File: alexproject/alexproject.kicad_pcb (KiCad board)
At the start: 2 copper layers, 22.4 x 27.9 mm, 20 parts, among them J1 Conn_01x03_Pin, Q1 NMOS, Q2 NMOS

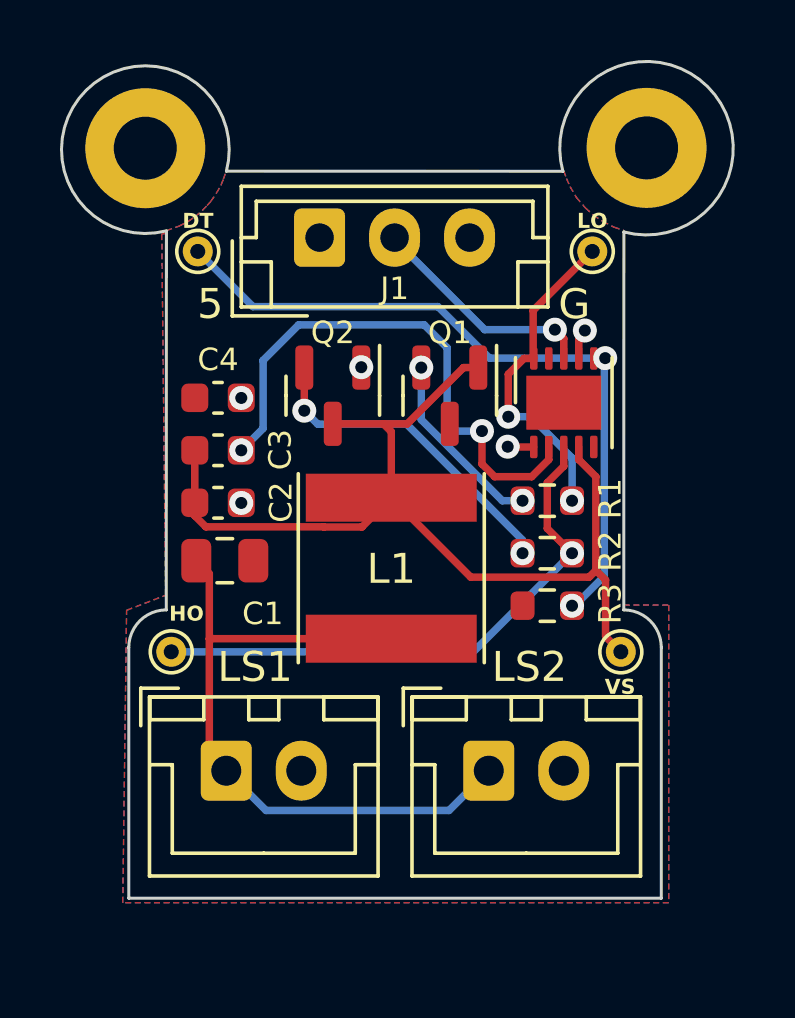
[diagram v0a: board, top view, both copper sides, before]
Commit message: testing spice sim & updated PCB
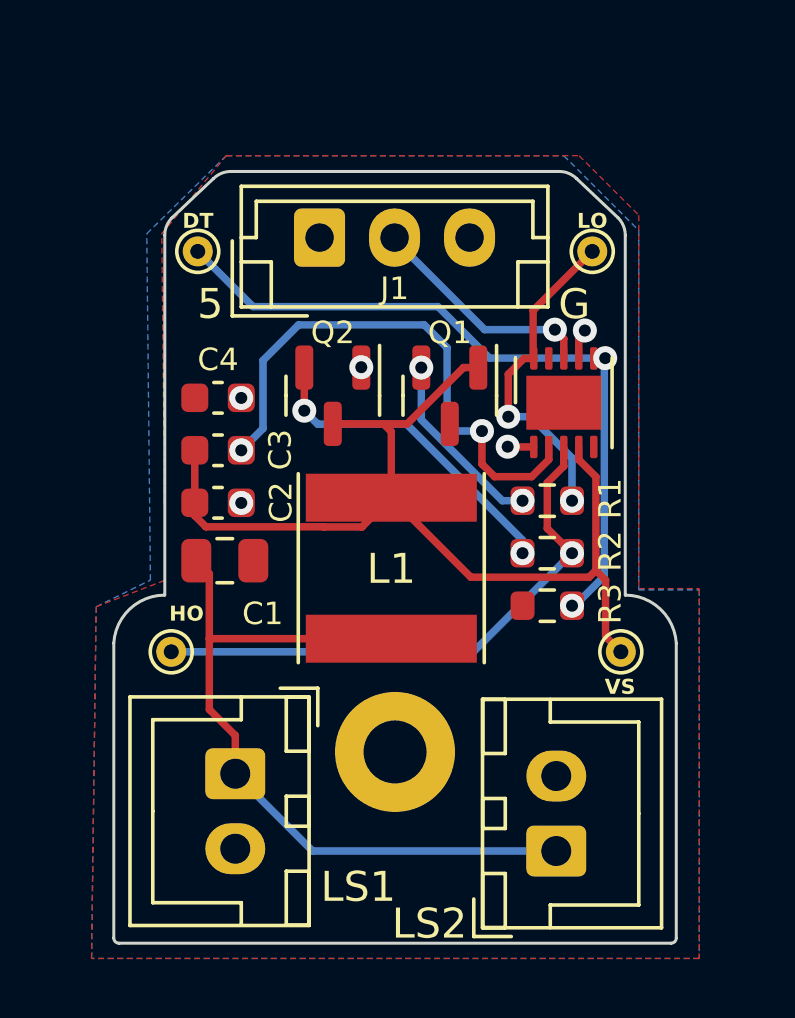
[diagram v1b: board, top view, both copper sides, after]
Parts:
- removed the REF** at (120.8, 57.0)
- moved REF** 21.8 mm to (129.1, 77.1)
- moved LS2 3.50 mm to (134.5, 80.4), turned to 90 degrees
- moved LS1 0.32 mm to (123.8, 77.8), turned to -90 degrees
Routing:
- net Net-(C1-Pad1): track 23.3 -> 25.5 mm
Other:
- board size 22.4 x 27.9 mm -> 18.8 x 25.7 mm
